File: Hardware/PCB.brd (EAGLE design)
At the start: 170.2 x 111.2 mm, 102 parts, among them IC1 BD5229G-TR, IC4 XC6220A331MR-G, J1 FH34SRJ-24S-0.5SH_99_, J2 SAMACSYS_PARTS_USB4110-GF-A, J3 QWIIC_RIGHT_ANGLE, J4 112A-TAAR-R03_ATTEND, Q1 20V/4.2A/52mΩ/1.4W, Q2 20V/4.2A/52mΩ/1.4W, Q3 SI1308EDL-T1-GE3, U1 W25Q512JVEIQ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

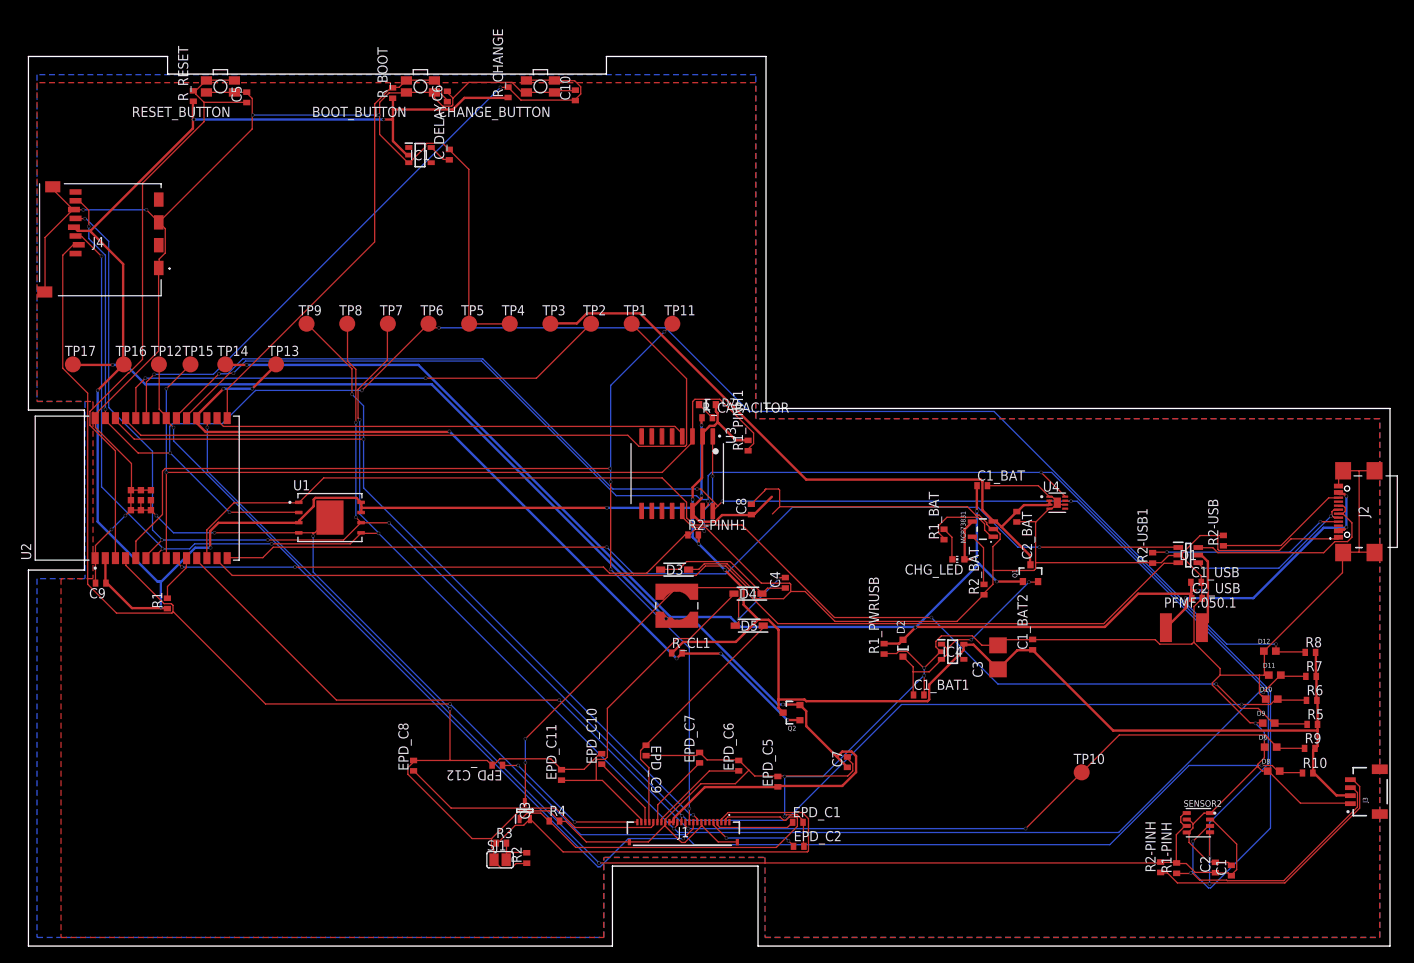
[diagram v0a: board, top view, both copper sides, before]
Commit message: Fixed PCB design.
Fixed overlapping errors with L1 and via.

Signed-off-by: Andrei Stan <standrei2003@yahoo.com>
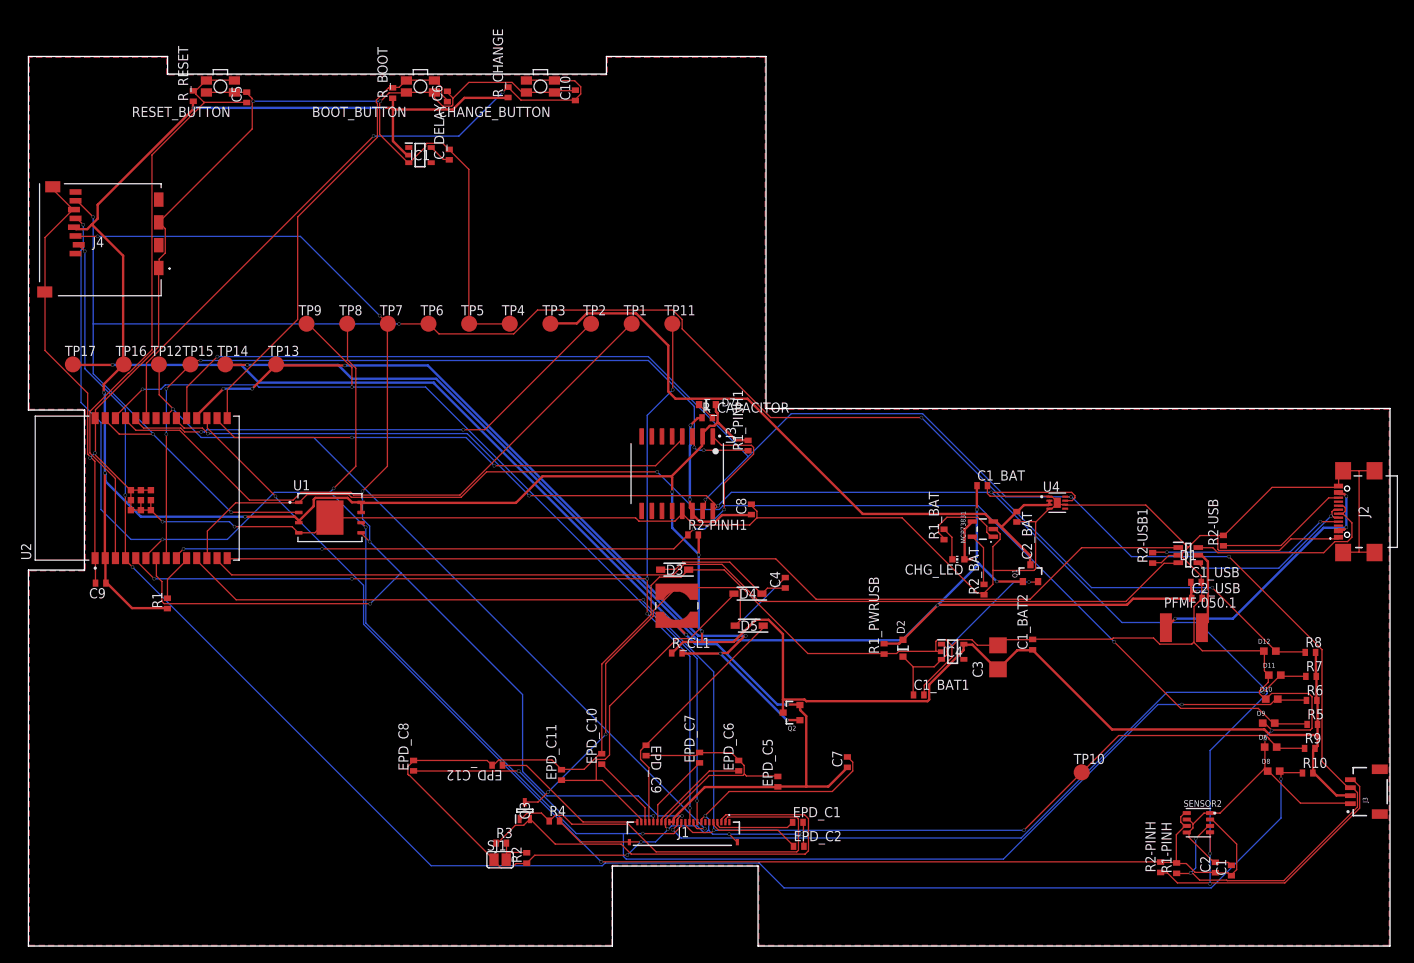
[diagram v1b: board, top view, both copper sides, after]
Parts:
- R3: value (none) -> 0.47
- SJ1: value (none) -> 0
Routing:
- net GND: track 771.4 -> 809.7 mm, vias 16 -> 14
- net SCK: track 240.7 -> 263.8 mm, vias 8 -> 6
- net MOSI: track 242.9 -> 260.7 mm, vias 7 -> 8
- net EPD_CS: track 159.2 -> 174.5 mm
- net TX: track 89.8 -> 77.0 mm
- net SS_SD: track 224.6 -> 216.0 mm, vias 2 -> 4
- net MISO: track 226.4 -> 234.2 mm, vias 7 -> 6
- net EPD_DC: track 138.0 -> 131.1 mm, vias 5 -> 6
- net SCL: track 223.0 -> 228.6 mm
- net INT_RTC: track 109.9 -> 104.6 mm, vias 2 -> 5
- net EPD_3V3: track 151.5 -> 146.2 mm
- net EPD_BUSY: track 115.0 -> 119.6 mm
- net 32KHZ: track 81.7 -> 86.1 mm
- net EPD_3V3_C: track 105.0 -> 108.0 mm
- net RTC_RST: track 59.4 -> 62.5 mm, vias 0 -> 2
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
